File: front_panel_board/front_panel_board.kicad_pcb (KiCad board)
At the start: 2 copper layers, 7 parts, among them J1 Conn_01x02_Male, J2 Conn_02x05_Odd_Even, SW1 SW_Rotary12_Letter

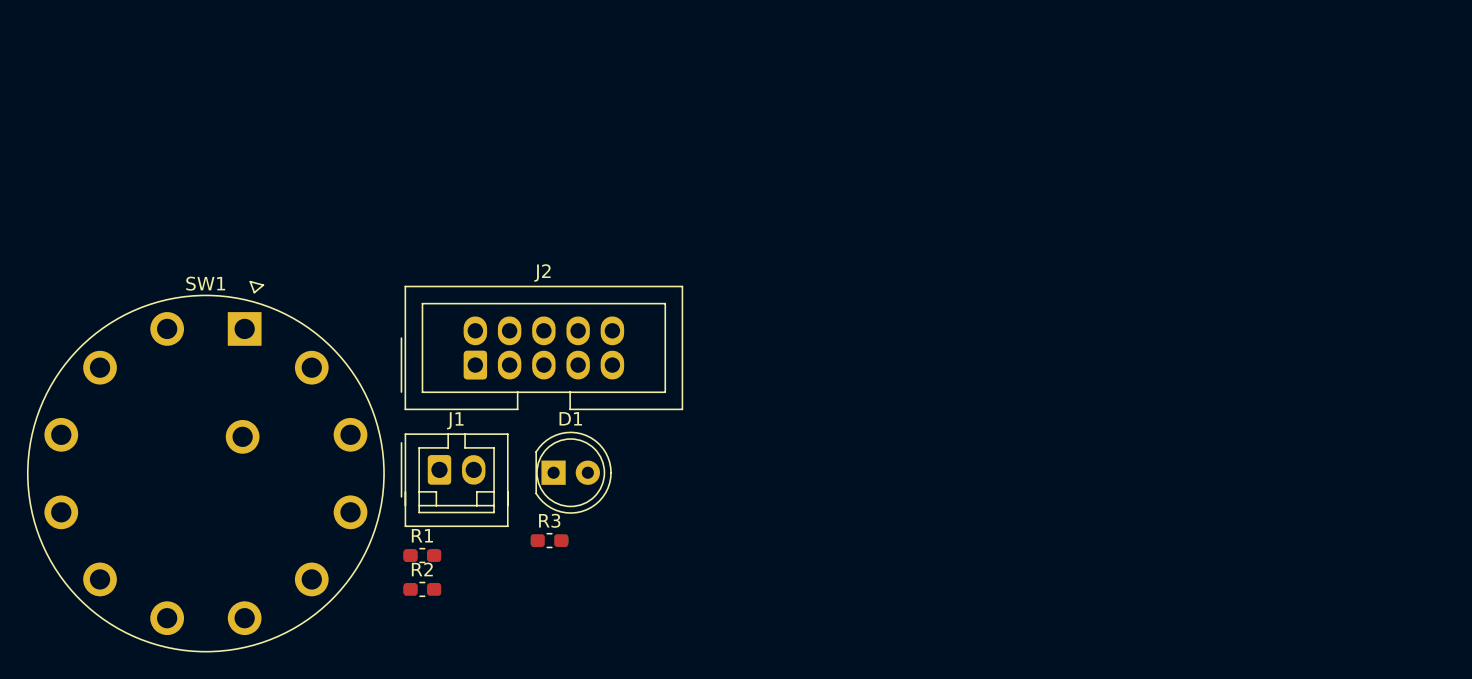
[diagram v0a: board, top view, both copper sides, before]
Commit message: add footprint for toggle switch and do inital layout (exact switch/LED placement tbd)
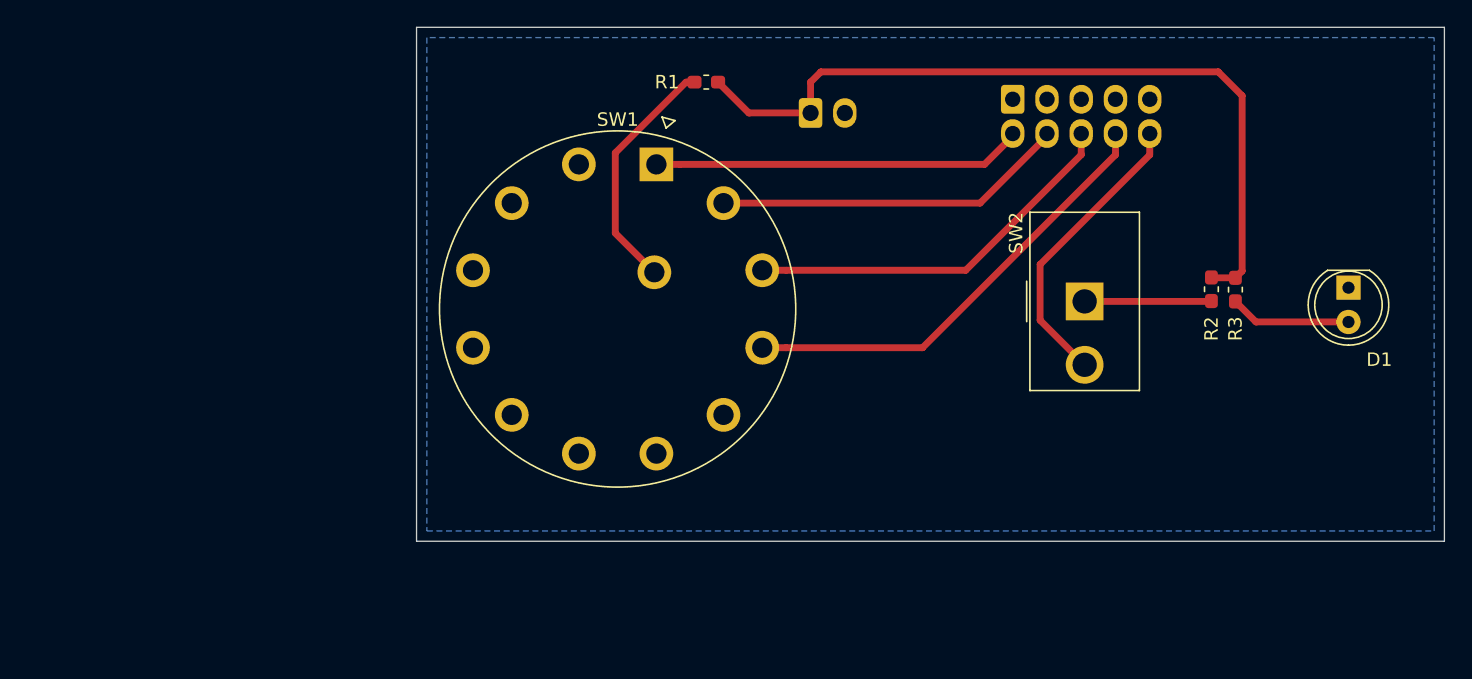
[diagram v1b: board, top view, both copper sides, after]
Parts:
- added SW2: SW_SPST, Button_Switch_THT_gkeeth:SW_Toggle_SPST_NKK_M2011xxx03, F.Cu at (151.1, 71.1)
- J1, J2: moved to B.Cu
- moved R2 62.6 mm to (160.5, 70.2), turned to 270 degrees
- moved D1 60.5 mm to (170.7, 70.1), turned to 270 degrees
- moved R3 54.1 mm to (162.3, 70.2), turned to 270 degrees
- moved J2 44.4 mm to (145.8, 56.1)
- moved R1 40.9 mm to (123.1, 54.9), turned to 180 degrees
- moved J1 38.2 mm to (130.8, 57.1)
- moved SW1 32.9 mm to (119.4, 61.0)
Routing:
- net Vrelay: track 0.00 -> 58.6 mm
- net /input4_select: track 0.00 -> 33.7 mm
- net /input3_select: track 0.00 -> 28.8 mm
- net /input1_select: track 0.00 -> 27.5 mm
- net /input2_select: track 0.00 -> 26.2 mm
- net /output_mute_select: track 0.00 -> 21.9 mm
- net Net-(R1-Pad2): track 0.00 -> 18.1 mm
- net Net-(R2-Pad2): track 0.00 -> 9.41 mm
- net Net-(D1-Pad2): track 0.00 -> 9.01 mm
- added copper zone on B.Cu, net GNDRELAY
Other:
- board outline added: 76.2 x 38.1 mm
- net class relay_power added: clearance 0.4, trace_width 0.508, via_dia 0.8, via_drill 0.4

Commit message: resize board slightly (to metric dims) and add project/license info to pcb
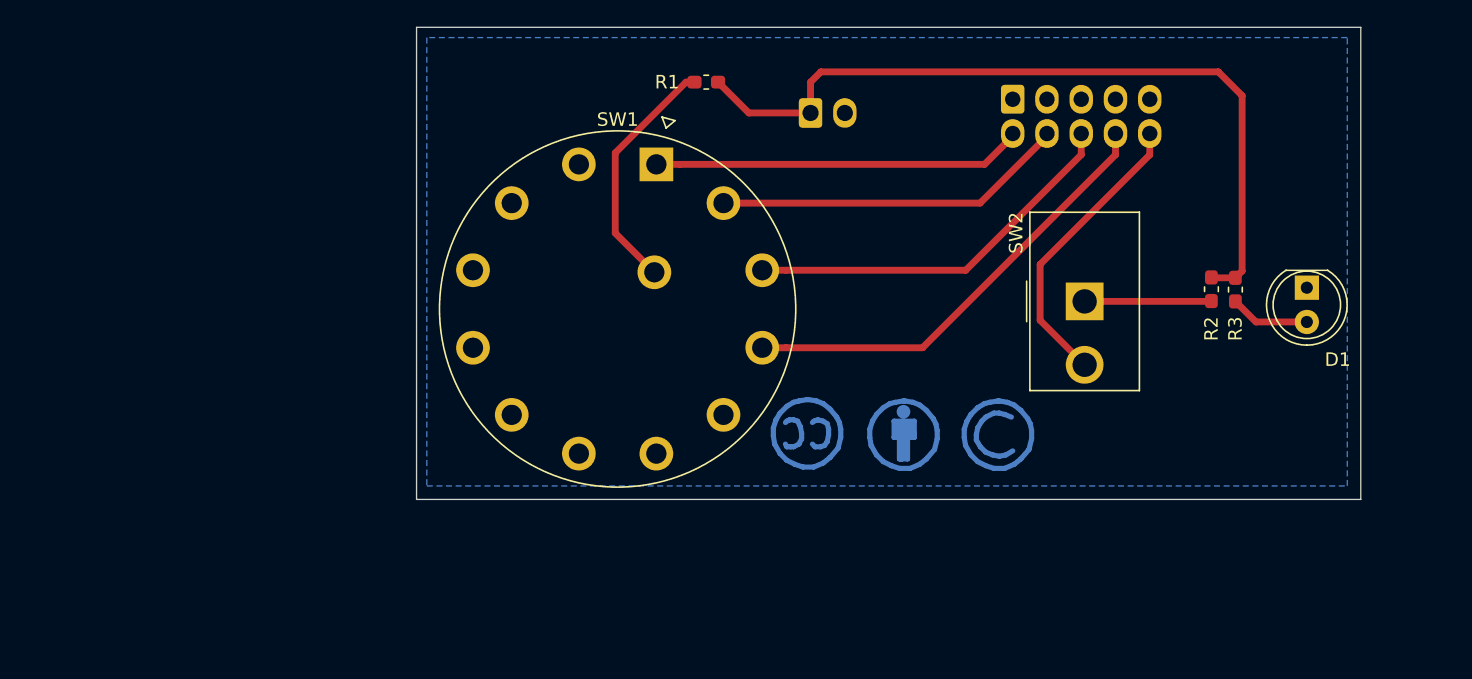
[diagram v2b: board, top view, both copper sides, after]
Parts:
- added REF**: Symbol_CC-ShareAlike_CopperTop_Small, Symbol:Symbol_CC-ShareAlike_CopperTop_Small, B.Cu at (144.7, 81.0)
- added REF**: Symbol_CC-Attribution_CopperTop_Small, Symbol:Symbol_CC-Attribution_CopperTop_Small, B.Cu at (137.7, 81.0)
- added REF**: Symbol_CreativeCommons_CopperTop_Type2_Small, Symbol:Symbol_CreativeCommons_CopperTop_Type2_Small, B.Cu at (130.7, 81.0)
- added REF**: OSHW-Symbol_6.7x6mm_SilkScreen, Symbol:OSHW-Symbol_6.7x6mm_SilkScreen, B.Cu at (166.6, 54.8)
- added REF**: KiCad-Logo2_5mm_SilkScreen, Symbol:KiCad-Logo2_5mm_SilkScreen, B.Cu at (109.6, 54.8)
- moved D1 3.09 mm to (167.6, 70.1)
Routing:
- net Net-(D1-Pad2): track 9.01 -> 5.93 mm
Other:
- board size 76.2 x 38.1 mm -> 70 x 35 mm
- board text added: "Front Panel Board rev0 Preamp 2019 G. Keeth 2019-06-09"
- board text added: "https://creativecommons.org/licenses/by-sa/4.0/"
